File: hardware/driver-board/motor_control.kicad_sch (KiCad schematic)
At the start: 16 parts, among them J1 CONN_MOTOR_L, J2 CONN_MOTOR_R, U1 DRV8838, U2 DRV8838

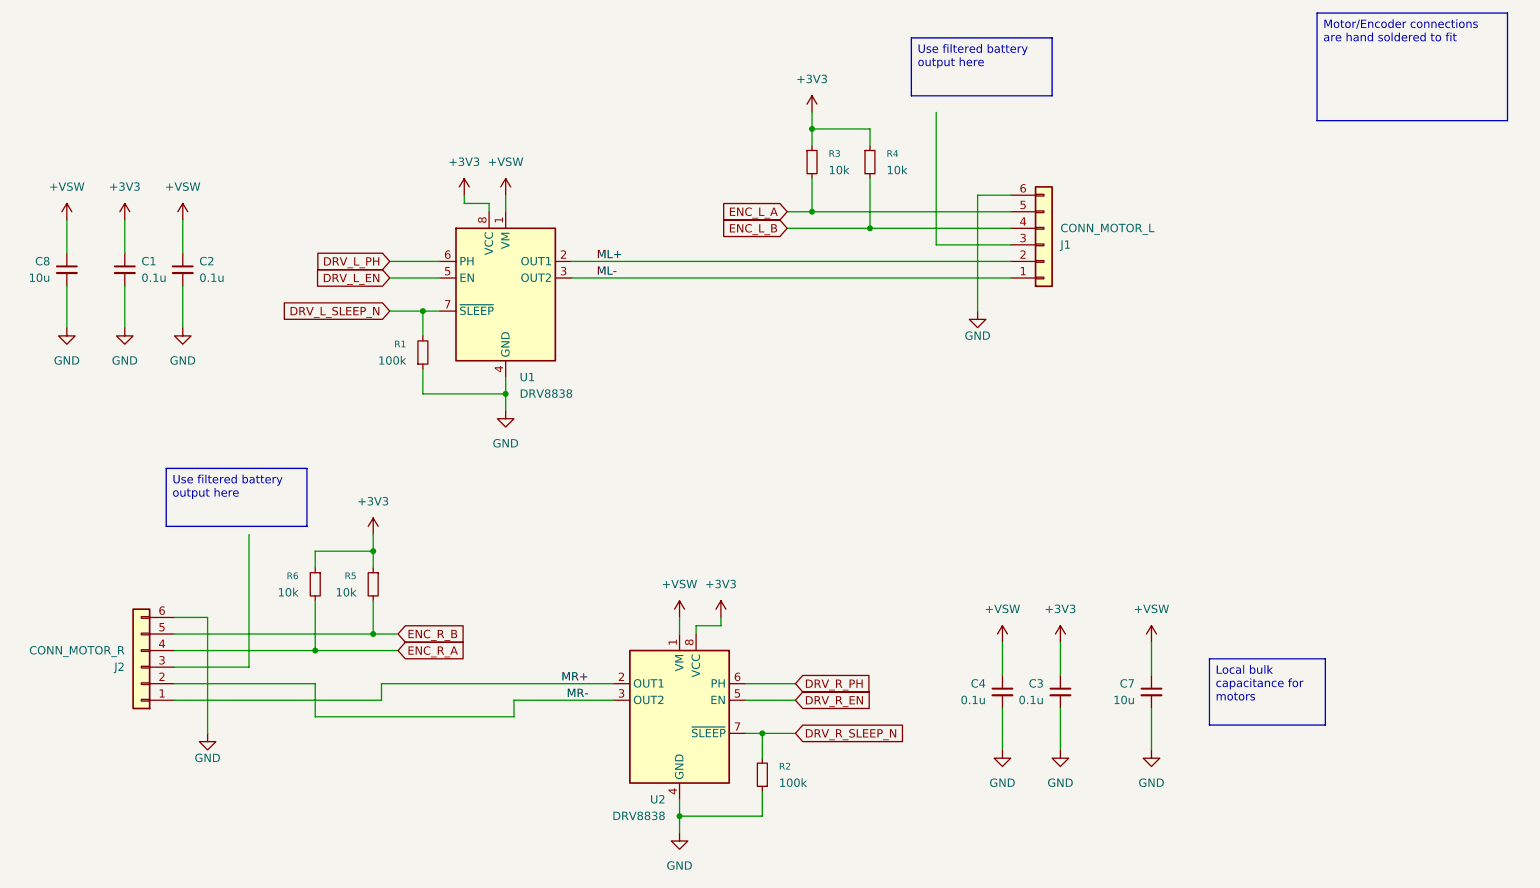
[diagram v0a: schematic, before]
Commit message: Checkpoint driver board schematic
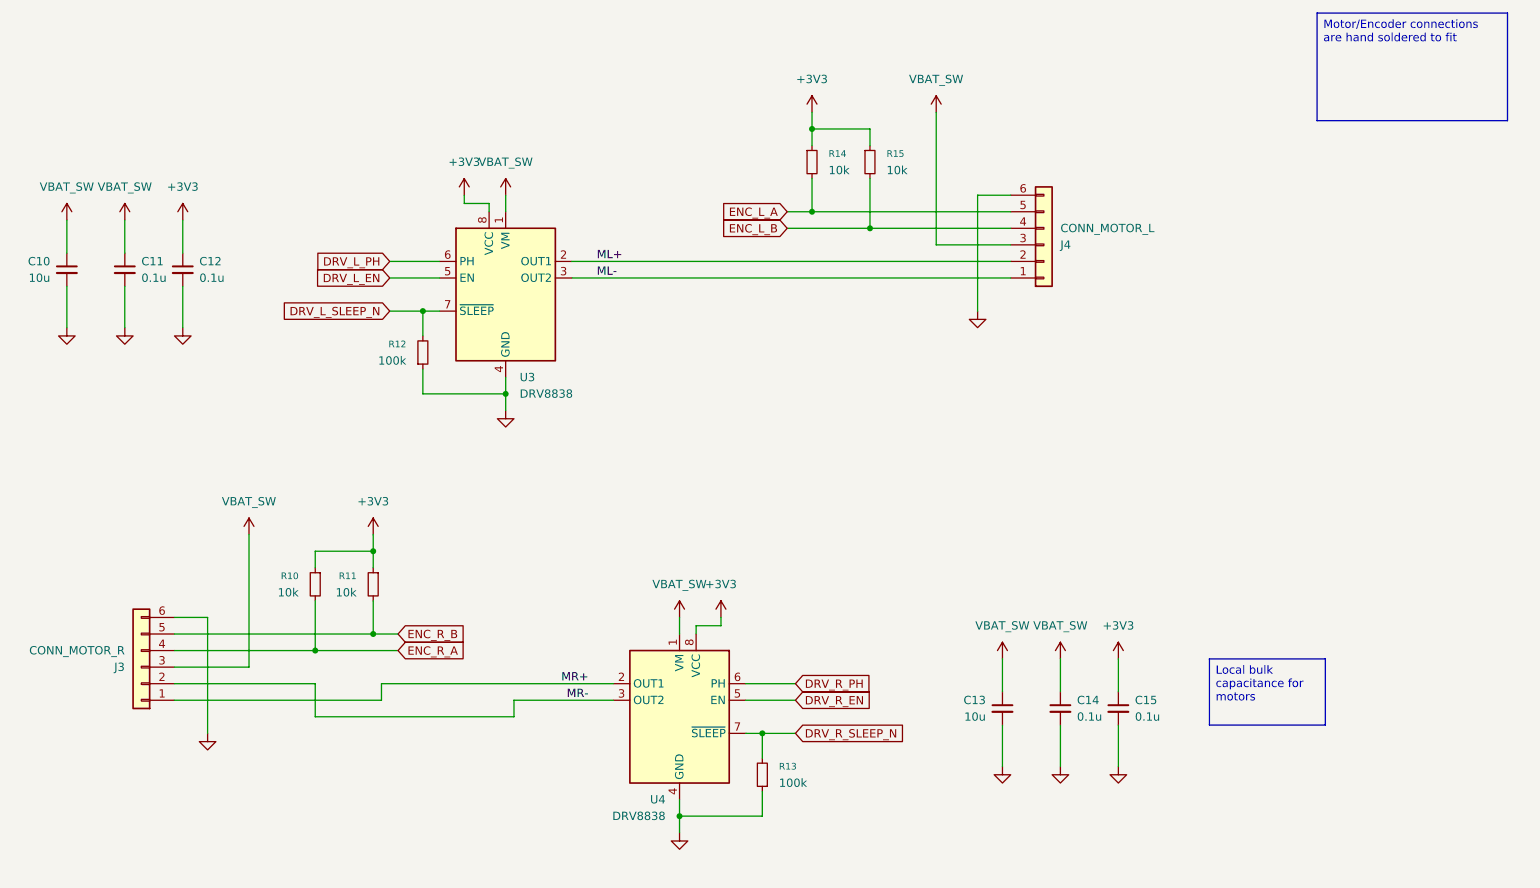
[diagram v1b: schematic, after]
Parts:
- removed C3, C4: 0.1u, Capacitor_SMD:C_0201_0603Metric, symbol Device:C_Small
- removed C7: 10u, Capacitor_SMD:C_1206_3216Metric, symbol Device:C_Small
- added C13: 10u, Capacitor_SMD:C_1206_3216Metric, symbol Device:C_Small
- added C14, C15: 0.1u, Capacitor_SMD:C_0201_0603Metric, symbol Device:C_Small
- renumbered C8 to C10, C1 to C11, C2 to C12, J2 to J3, J1 to J4, R6 to R10, R5 to R11, R1 to R12, R2 to R13, R3 to R14, R4 to R15, U1 to U3, U2 to U4
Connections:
- net +3V3: now also C12.1, C15.1; no longer C11.1
- net GND: now also C13.2, C14.2, C15.2
- net VBAT_SW: now reaches J4.3 (Pin_3)
- net VBAT_SW: now also C10.1, C11.1, J3.3 (Pin_3), U3.1 (VM), U4.1 (VM), C13.1, C14.1
- removed net +VSW: C10.1, C12.1, U3.1 (VM), U4.1 (VM)

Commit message: Wrap up Rev A schematic pre-layout tasks
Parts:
- C10, C13: JLCPCB C76661 -> C13585; JLCPCB Type (none) -> Basic
- C11, C12, C14, C15: value 0.1u -> 100n; footprint Capacitor_SMD:C_0201_0603Metric -> Capacitor_SMD:C_0603_1608Metric; JLCPCB (none) -> C14663; JLCPCB Type (none) -> Basic
- J3, J4: footprint (none) -> Connector_PinSocket_2.54mm:PinSocket_1x06_P2.54mm_Vertical
- R10, R11, R14, R15: footprint (none) -> Resistor_SMD:R_0603_1608Metric; JLCPCB (none) -> C25804; JLCPCB Type (none) -> Basic
- R12, R13: footprint Resistor_SMD:R_0201_0603Metric -> Resistor_SMD:R_0603_1608Metric; JLCPCB (none) -> C25803; JLCPCB Type (none) -> Basic

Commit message: Complete Romi-compatible board placement and power switching
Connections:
- net ENC_R_A: now also J3.3 (Pin_3); no longer J3.4 (Pin_4)
- net ENC_R_B: now also J3.2 (Pin_2); no longer J3.5 (Pin_5)
- net GND: now also J3.1 (Pin_1); no longer J3.6 (Pin_6)
- net MR+: now also J3.6 (Pin_6); no longer J3.1 (Pin_1)
- net MR-: now also J3.5 (Pin_5); no longer J3.2 (Pin_2)
- net VBAT_SW: now also J3.4 (Pin_4); no longer J3.3 (Pin_3)
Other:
- moved on the sheet: J3

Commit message: Refine driver board placement and capacitor footprints
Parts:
- C10, C13: footprint Capacitor_SMD:C_1206_3216Metric -> Capacitor_SMD:C_0805_2012Metric; JLCPCB C13585 -> C15850
- C11, C12, C14, C15: footprint Capacitor_SMD:C_0603_1608Metric -> Capacitor_SMD:C_0402_1005Metric; JLCPCB C14663 -> C307331
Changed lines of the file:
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@@
 			)
 		)
-		(property "Footprint" "Capacitor_SMD:C_0603_1608Metric"
+		(property "Footprint" "Capacitor_SMD:C_0402_1005Metric"
 			(at 63.5 60.96 0)
 			(hide yes)
@@
 			)
 		)
-		(property "JLCPCB" "C14663"
+		(property "JLCPCB" "C307331"
 			(at 63.5 60.96 0)
 			(hide yes)
@@
 			)
 		)
-		(property "Footprint" "Capacitor_SMD:C_0603_1608Metric"
+		(property "Footprint" "Capacitor_SMD:C_0402_1005Metric"
 			(at 198.12 128.27 0)
 			(hide yes)
@@
 			)
 		)
-		(property "JLCPCB" "C14663"
+		(property "JLCPCB" "C307331"
 			(at 198.12 128.27 0)
 			(hide yes)
@@
 			)
 		)
-		(property "Footprint" "Capacitor_SMD:C_0603_1608Metric"
+		(property "Footprint" "Capacitor_SMD:C_0402_1005Metric"
 			(at 54.61 60.96 0)
 			(hide yes)
@@
 			)
 		)
-		(property "JLCPCB" "C14663"
+		(property "JLCPCB" "C307331"
 			(at 54.61 60.96 0)
 			(hide yes)
@@
 			)
 		)
-		(property "Footprint" "Capacitor_SMD:C_0603_1608Metric"
+		(property "Footprint" "Capacitor_SMD:C_0402_1005Metric"
 			(at 207.01 128.27 0)
 			(hide yes)
@@
 			)
 		)
-		(property "JLCPCB" "C14663"
+		(property "JLCPCB" "C307331"
 			(at 207.01 128.27 0)
 			(hide yes)
@@
 			)
 		)
-		(property "Footprint" "Capacitor_SMD:C_1206_3216Metric"
+		(property "Footprint" "Capacitor_SMD:C_0805_2012Metric"
 			(at 189.23 128.27 0)
 			(hide yes)
@@
 			)
 		)
-		(property "JLCPCB" "C13585"
+		(property "JLCPCB" "C15850"
 			(at 189.23 128.27 0)
 			(hide yes)
@@
 			)
 		)
-		(property "Footprint" "Capacitor_SMD:C_1206_3216Metric"
+		(property "Footprint" "Capacitor_SMD:C_0805_2012Metric"
 			(at 45.72 60.96 0)
 			(hide yes)
@@
 			)
 		)
-		(property "JLCPCB" "C13585"
+		(property "JLCPCB" "C15850"
 			(at 45.72 60.96 0)
 			(hide yes)

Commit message: Refine driver board placement and motor power checks
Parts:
- R10, R11, R14, R15: footprint Resistor_SMD:R_0603_1608Metric -> Resistor_SMD:R_0402_1005Metric; JLCPCB C25804 -> C25744
- R12, R13: footprint Resistor_SMD:R_0603_1608Metric -> Resistor_SMD:R_0402_1005Metric; JLCPCB C25803 -> (none)
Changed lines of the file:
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@@
 			)
 		)
-		(property "Footprint" "Resistor_SMD:R_0603_1608Metric"
+		(property "Footprint" "Resistor_SMD:R_0402_1005Metric"
 			(at 152.4 138.43 0)
 			(hide yes)
@@
 			)
 		)
-		(property "JLCPCB" "C25803"
+		(property "JLCPCB" ""
 			(at 152.4 138.43 0)
 			(hide yes)
@@
 			)
 		)
-		(property "Footprint" "Resistor_SMD:R_0603_1608Metric"
+		(property "Footprint" "Resistor_SMD:R_0402_1005Metric"
 			(at 92.71 109.22 0)
 			(hide yes)
@@
 			)
 		)
-		(property "JLCPCB" "C25804"
+		(property "JLCPCB" "C25744"
 			(at 92.71 109.22 0)
 			(hide yes)
@@
 			)
 		)
-		(property "Footprint" "Resistor_SMD:R_0603_1608Metric"
+		(property "Footprint" "Resistor_SMD:R_0402_1005Metric"
 			(at 83.82 109.22 0)
 			(hide yes)
@@
 			)
 		)
-		(property "JLCPCB" "C25804"
+		(property "JLCPCB" "C25744"
 			(at 83.82 109.22 0)
 			(hide yes)
@@
 			)
 		)
-		(property "Footprint" "Resistor_SMD:R_0603_1608Metric"
+		(property "Footprint" "Resistor_SMD:R_0402_1005Metric"
 			(at 160.02 44.45 0)
 			(hide yes)
@@
 			)
 		)
-		(property "JLCPCB" "C25804"
+		(property "JLCPCB" "C25744"
 			(at 160.02 44.45 0)
 			(hide yes)
@@
 			)
 		)
-		(property "Footprint" "Resistor_SMD:R_0603_1608Metric"
+		(property "Footprint" "Resistor_SMD:R_0402_1005Metric"
 			(at 168.91 44.45 0)
 			(hide yes)
@@
 			)
 		)
-		(property "JLCPCB" "C25804"
+		(property "JLCPCB" "C25744"
 			(at 168.91 44.45 0)
 			(hide yes)
@@
 			)
 		)
-		(property "Footprint" "Resistor_SMD:R_0603_1608Metric"
+		(property "Footprint" "Resistor_SMD:R_0402_1005Metric"
 			(at 100.33 73.66 0)
 			(hide yes)
@@
 			)
 		)
-		(property "JLCPCB" "C25803"
+		(property "JLCPCB" ""
 			(at 100.33 73.66 0)
 			(hide yes)

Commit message: Refine Rev A PCB placement and decoupling
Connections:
- net ML+: now also J4.1 (Pin_1); no longer J4.2 (Pin_2)
- net ML-: now also J4.2 (Pin_2); no longer J4.1 (Pin_1)
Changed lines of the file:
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@@
+	(wire
+		(pts
+			(xy 160.02 62.23) (xy 190.5 62.23)
+		)
+		(stroke
+			(width 0)
+			(type default)
+		)
+	)
 	(wire
 		(pts
@@
 	(wire
 		(pts
+			(xy 156.21 57.15) (xy 163.83 57.15)
+		)
+		(stroke
+			(width 0)
+			(type default)
+		)
+	)
+	(wire
+		(pts
 			(xy 190.5 49.53) (xy 185.42 49.53)
 		)
@@
 	(wire
 		(pts
+			(xy 160.02 59.69) (xy 160.02 62.23)
+		)
+		(stroke
+			(width 0)
+			(type default)
+		)
+	)
+	(wire
+		(pts
 			(xy 157.48 132.08) (xy 152.4 132.08)
 		)
@@
 	(wire
 		(pts
+			(xy 123.19 62.23) (xy 156.21 62.23)
+		)
+		(stroke
+			(width 0)
+			(type default)
+		)
+	)
+	(wire
+		(pts
 			(xy 146.05 115.57) (xy 146.05 114.3)
 		)
@@
 	(wire
 		(pts
-			(xy 123.19 59.69) (xy 190.5 59.69)
-		)
-		(stroke
-			(width 0)
-			(type default)
-		)
-	)
-	(wire
-		(pts
 			(xy 113.03 80.01) (xy 113.03 82.55)
 		)
@@
 	(wire
 		(pts
+			(xy 163.83 57.15) (xy 163.83 59.69)
+		)
+		(stroke
+			(width 0)
+			(type default)
+		)
+	)
+	(wire
+		(pts
 			(xy 156.21 52.07) (xy 160.02 52.07)
 		)
@@
 	(wire
 		(pts
+			(xy 163.83 59.69) (xy 190.5 59.69)
+		)
+		(stroke
+			(width 0)
+			(type default)
+		)
+	)
+	(wire
+		(pts
 			(xy 62.23 114.3) (xy 67.31 114.3)
 		)
@@
 	(wire
 		(pts
+			(xy 156.21 62.23) (xy 156.21 57.15)
+		)
+		(stroke
+			(width 0)
+			(type default)
+		)
+	)
+	(wire
+		(pts
 			(xy 92.71 116.84) (xy 92.71 111.76)
 		)
@@
 	(wire
 		(pts
+			(xy 123.19 59.69) (xy 160.02 59.69)
+		)
+		(stroke
+			(width 0)
+			(type default)
+		)
+	)
+	(wire
+		(pts
 			(xy 160.02 52.07) (xy 190.5 52.07)
 		)
 		(stroke
-			(width 0)
-			(type default)
-		)
-	)
-	(wire
-		(pts
-			(xy 123.19 62.23) (xy 190.5 62.23)
-		)
-		(stroke

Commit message: Checkpoint left driver and firmware pin mapping
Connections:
- net ML+: now also J4.2 (Pin_2); no longer J4.1 (Pin_1)
- net ML-: now also J4.1 (Pin_1); no longer J4.2 (Pin_2)
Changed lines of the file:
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@@
-	(wire
-		(pts
-			(xy 160.02 62.23) (xy 190.5 62.23)
-		)
-		(stroke
-			(width 0)
-			(type default)
-		)
-	)
 	(wire
 		(pts
@@
 	(wire
 		(pts
-			(xy 156.21 57.15) (xy 163.83 57.15)
-		)
-		(stroke
-			(width 0)
-			(type default)
-		)
-	)
-	(wire
-		(pts
 			(xy 190.5 49.53) (xy 185.42 49.53)
 		)
@@
 	(wire
 		(pts
-			(xy 160.02 59.69) (xy 160.02 62.23)
-		)
-		(stroke
-			(width 0)
-			(type default)
-		)
-	)
-	(wire
-		(pts
 			(xy 157.48 132.08) (xy 152.4 132.08)
 		)
@@
 	(wire
 		(pts
-			(xy 123.19 62.23) (xy 156.21 62.23)
+			(xy 123.19 62.23) (xy 190.5 62.23)
 		)
 		(stroke
@@
 	(wire
 		(pts
-			(xy 163.83 57.15) (xy 163.83 59.69)
-		)
-		(stroke
-			(width 0)
-			(type default)
-		)
-	)
-	(wire
-		(pts
 			(xy 156.21 52.07) (xy 160.02 52.07)
 		)
@@
 	(wire
 		(pts
-			(xy 163.83 59.69) (xy 190.5 59.69)
-		)
-		(stroke
-			(width 0)
-			(type default)
-		)
-	)
-	(wire
-		(pts
 			(xy 62.23 114.3) (xy 67.31 114.3)
 		)
@@
 	(wire
 		(pts
-			(xy 156.21 62.23) (xy 156.21 57.15)
-		)
-		(stroke
-			(width 0)
-			(type default)
-		)
-	)
-	(wire
-		(pts
 			(xy 92.71 116.84) (xy 92.71 111.76)
 		)
@@
 	(wire
 		(pts
-			(xy 123.19 59.69) (xy 160.02 59.69)
-		)
-		(stroke
+			(xy 123.19 59.69) (xy 190.5 59.69)
+		)
+		(stroke

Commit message: Complete motor driver layouts and pin mapping
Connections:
- net MR+: now also J3.5 (Pin_5); no longer J3.6 (Pin_6)
- net MR-: now also J3.6 (Pin_6); no longer J3.5 (Pin_5)
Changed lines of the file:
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@@
-	(wire
-		(pts
-			(xy 83.82 124.46) (xy 83.82 129.54)
-		)
-		(stroke
-			(width 0)
-			(type default)
-		)
-	)
 	(wire
 		(pts
@@
 	(wire
 		(pts
-			(xy 129.54 124.46) (xy 93.98 124.46)
-		)
-		(stroke
-			(width 0)
-			(type default)
-		)
-	)
-	(wire
-		(pts
-			(xy 62.23 124.46) (xy 83.82 124.46)
+			(xy 62.23 124.46) (xy 129.54 124.46)
 		)
 		(stroke
@@
 	(wire
 		(pts
-			(xy 114.3 129.54) (xy 114.3 127)
-		)
-		(stroke
-			(width 0)
-			(type default)
-		)
-	)
-	(wire
-		(pts
-			(xy 93.98 124.46) (xy 93.98 127)
-		)
-		(stroke
-			(width 0)
-			(type default)
-		)
-	)
-	(wire
-		(pts
 			(xy 152.4 132.08) (xy 152.4 135.89)
 		)
@@
 	(wire
 		(pts
-			(xy 114.3 127) (xy 129.54 127)
-		)
-		(stroke
-			(width 0)
-			(type default)
-		)
-	)
-	(wire
-		(pts
-			(xy 83.82 129.54) (xy 114.3 129.54)
-		)
-		(stroke
-			(width 0)
-			(type default)
-		)
-	)
-	(wire
-		(pts
 			(xy 96.52 119.38) (xy 83.82 119.38)
 		)
@@
 	(wire
 		(pts
-			(xy 93.98 127) (xy 62.23 127)
-		)
-		(stroke
+			(xy 62.23 127) (xy 129.54 127)
+		)
+		(stroke
